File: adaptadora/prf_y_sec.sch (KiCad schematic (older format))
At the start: 35 parts, among them J18 Conn_Coaxial, J19 Conn_Coaxial, J20 Conn_Coaxial, J22 Conn_Coaxial, U13 LM361MX_NOPB, U14 LM361MX_NOPB, U23 TLV2772IDR, U32 SN74LVC2T45DCUR

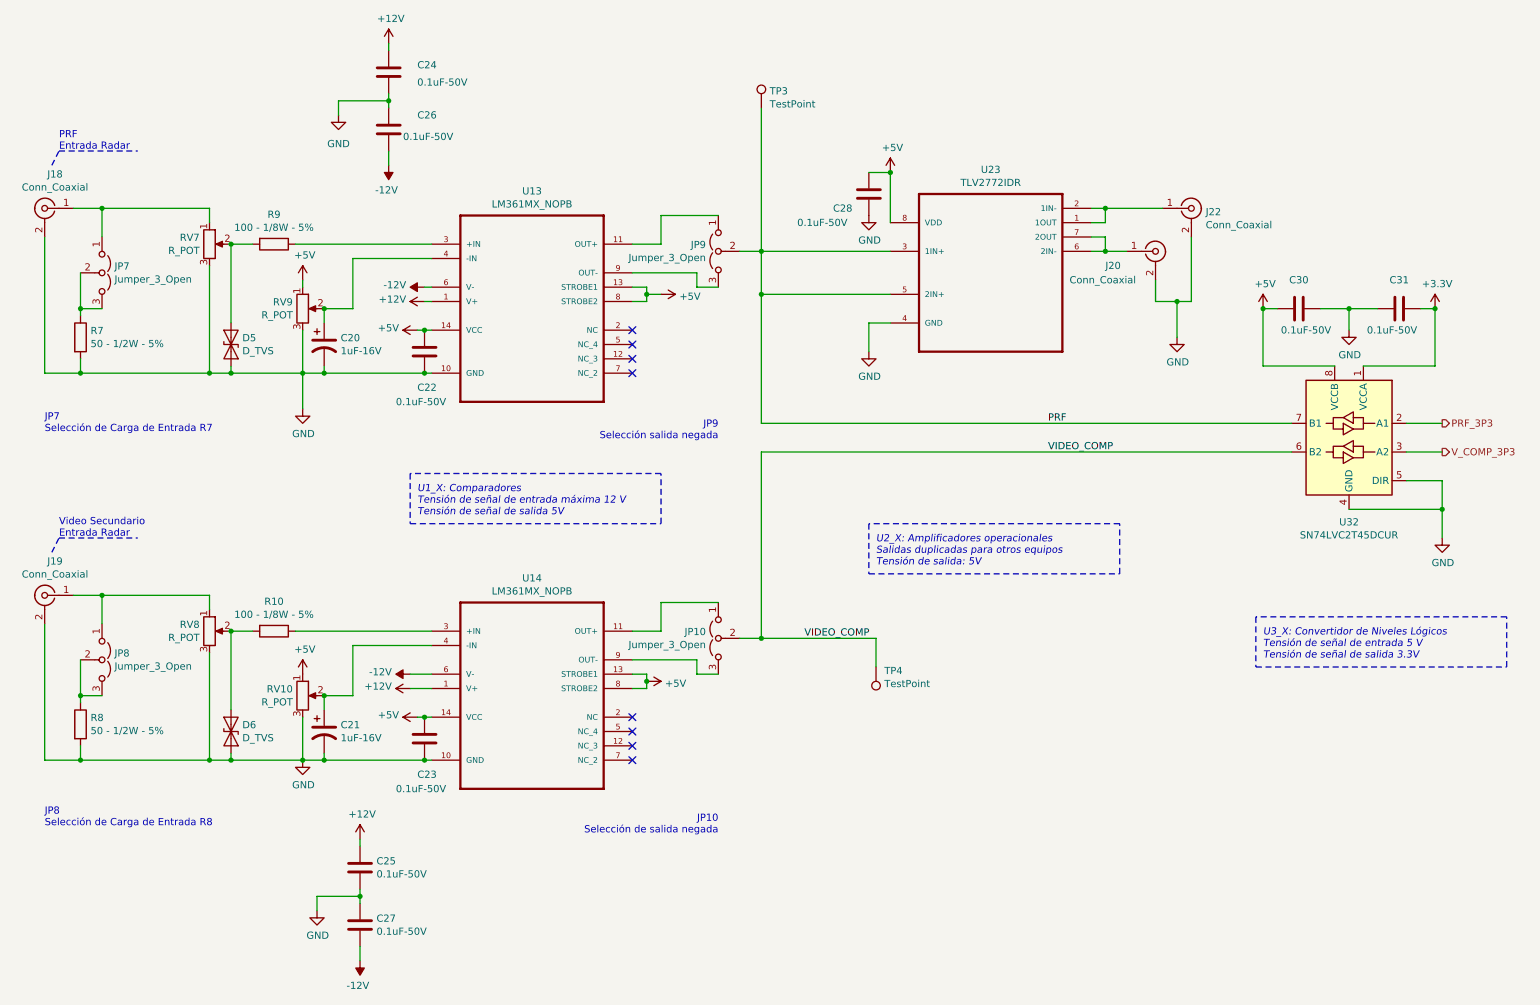
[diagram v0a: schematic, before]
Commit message: se ordenan campos de integrados
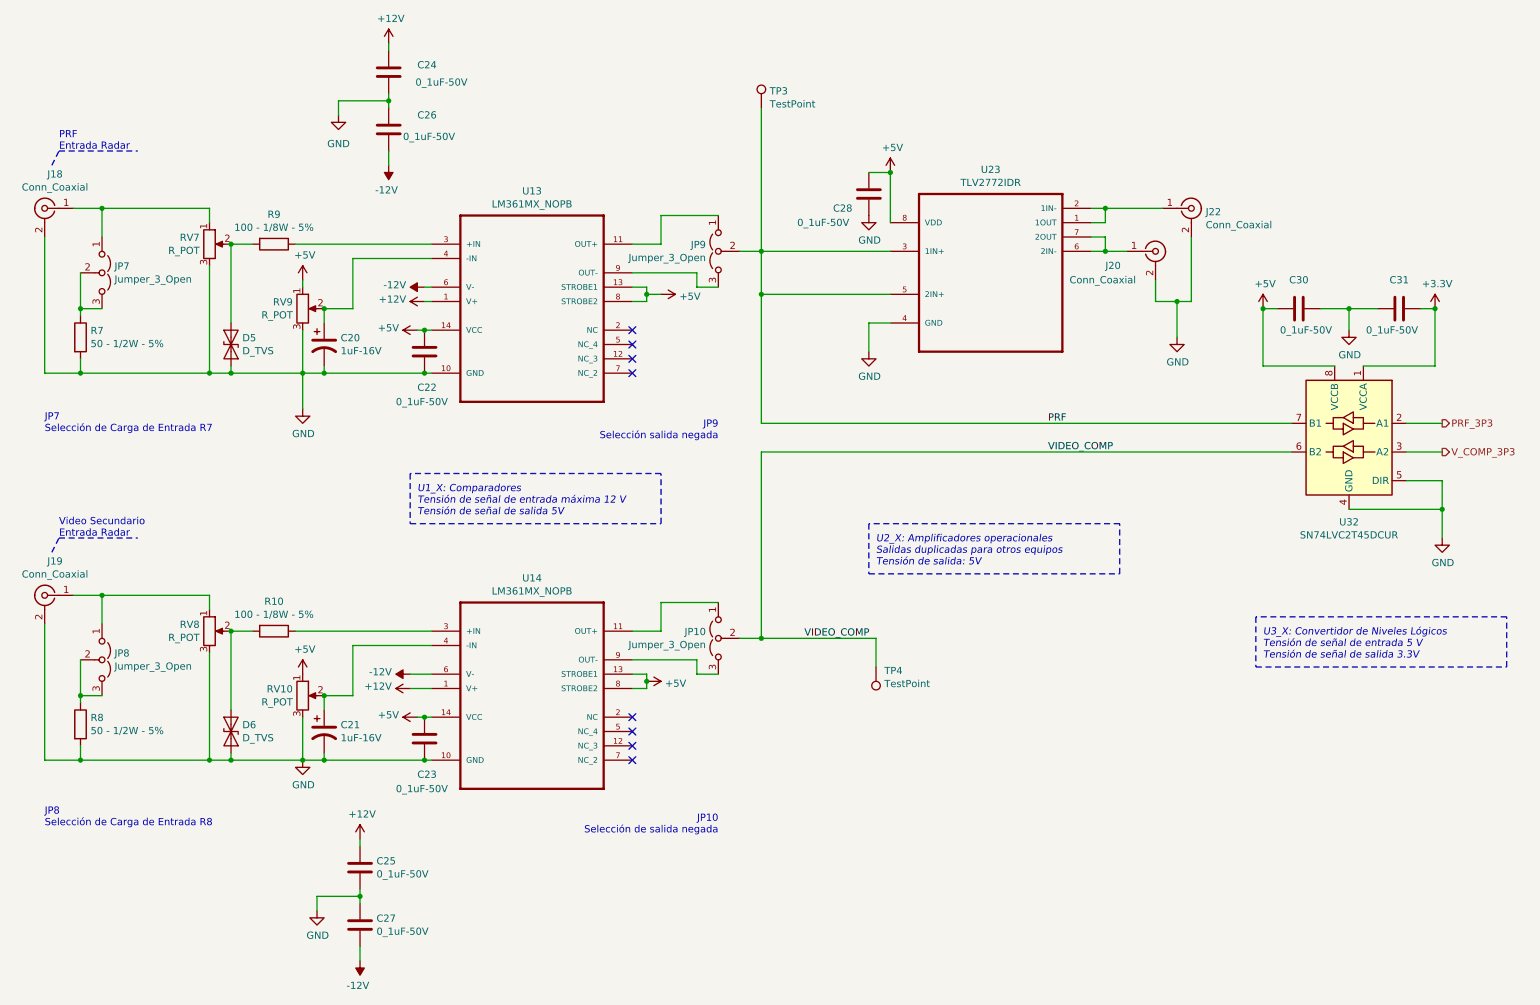
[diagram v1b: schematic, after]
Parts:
- C22, C23, C24, C25, C26, C27, C28, C30, C31: value 0.1uF-50V -> 0_1uF-50V
- U13, U14: Número de parte (Digi-Key) 296-47682-1-ND -> (none)
- U23: Campo4 Texas Instruments -> (none); Campo5 Dual 2.7-V High Slew Rate Rail-To-Rail Output Operational A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 -> (none); Campo6 TLV2772IDR -> (none); Campo7 https://www.digikey.com/product-detail/en/texas-instruments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 -> (none); Campo8 SOIC-8 Texas Instruments -> (none); Descripción (inglés) General Purpose Amplifier 2 Circuit Rail-to-Rail 8-SOIC -> Dual 2.7-V High Slew Rate Rail-To-Rail Output Operational A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; Número de parte (Digi-Key) 296-1902-2-ND -> (none)
- U32: Número de parte (Digi-Key) 296-17014-1-ND -> (none)
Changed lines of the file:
@@
 P 3350 2950
 F 0 "C22" H 3400 3200 50  0000 R CNN
-F 1 "0.1uF-50V" H 3550 3300 50  0000 R CNN
+F 1 "0_1uF-50V" H 3550 3300 50  0000 R CNN
 F 2 "Capacitor_SMD:C_0805_2012Metric" H 3388 2800 50  0001 C CNN
 F 3 "~" H 3350 2950 50  0001 C CNN
@@
 F 4 "Texas Instruments" H 4100 2500 50  0001 L BNN "Fabricante"
 F 5 "High Speed Differential Comparator 14-SOIC 0 to 70" H 4100 2500 50  0001 L BNN "Descripción (inglés)"
-F 6 "296-47682-1-ND" H 4100 2500 50  0001 L BNN "Número de parte (Digi-Key)"
+F 6 "296-47682-1-ND" H 4100 2500 50  0001 L BNN "Número de Parte (Digi-Key)"
 F 7 "https://www.digikey.com/product-detail/en/texas-instruments/LM361MX-NOPB/296-47682-1-ND/3526971" H 4100 2500 50  0001 L BNN "Enlace"
-F 8 "296-47682-1-ND" H 4100 2500 50  0001 C CNN "Número de Parte (Digi-Key)"
 	1    4100 2500
 	1    0    0    -1
@@
 P 3100 1000
 F 0 "C24" H 2900 1050 50  0000 R CNN
-F 1 "0.1uF-50V" H 2550 900 50  0000 L BNN
+F 1 "0_1uF-50V" H 2550 900 50  0000 L BNN
 F 2 "Capacitor_SMD:C_0805_2012Metric" H 3138 850 50  0001 C CNN
 F 3 "~" H 3100 1000 50  0001 C CNN
@@
 P 3100 1400
 F 0 "C26" H 3300 1500 50  0000 L CNN
-F 1 "0.1uF-50V" H 3200 1350 50  0000 L CNN
+F 1 "0_1uF-50V" H 3200 1350 50  0000 L CNN
 F 2 "Capacitor_SMD:C_0805_2012Metric" H 3138 1250 50  0001 C CNN
 F 3 "~" H 3100 1400 50  0001 C CNN
@@
 F 2 "Package_SO:SOIC-8_3.9x4.9mm_P1.27mm" H 7300 2250 50  0001 L BNN
 F 3 "http://www.ti.com/lit/ds/symlink/tlv2772.pdf" H 7300 2250 50  0001 L BNN
-F 4 "Texas Instruments" H 7300 2250 50  0001 L BNN "Campo4"
-F 5 "Dual 2.7-V High Slew Rate Rail-To-Rail Output Operational Amplifier 8-SOIC -40 to 125" H 7300 2250 50  0001 L BNN "Campo5"
-F 6 "TLV2772IDR" H 7300 2250 50  0001 L BNN "Campo6"
-F 7 "https://www.digikey.com/product-detail/en/texas-instruments/TLV2772IDR/296-1902-1-ND/405014?utm_source=snapeda&utm_medium=aggregator&utm_campaign=symbol" H 7300 2250 50  0001 L BNN "Campo7"
-F 8 "SOIC-8 Texas Instruments" H 7300 2250 50  0001 L BNN "Campo8"
-F 9 "General Purpose Amplifier 2 Circuit Rail-to-Rail 8-SOIC" H 7300 2250 50  0001 C CNN "Descripción (inglés)"
-F 10 "https://www.digikey.com/product-detail/en/texas-instruments/TLV2772IDR/296-1902-2-ND/374332" H 7300 2250 50  0001 C CNN "Enlace"
-F 11 "Texas Instruments" H 7300 2250 50  0001 C CNN "Fabricante"
-F 12 "296-1902-2-ND" H 7300 2250 50  0001 C CNN "Número de Parte (Digi-Key)"
-F 13 "296-1902-2-ND" H 7300 2250 50  0001 C CNN "Número de parte (Digi-Key)"
+F 4 "Dual 2.7-V High Slew Rate Rail-To-Rail Output Operational Amplifier 8-SOIC -40 to 125" H 7300 2250 50  0001 C CNN "Descripción (inglés)"
+F 5 "Texas Instruments" H 7300 2250 50  0001 C CNN "Fabricante"
+F 6 "296-1902-2-ND" H 7300 2250 50  0001 C CNN "Número de Parte (Digi-Key)"
+F 7 "https://www.digikey.com/product-detail/en/texas-instruments/TLV2772IDR/296-1902-2-ND/374332" H 7300 2250 50  0001 C CNN "Enlace"
 	1    7300 2250
 	1    0    0    -1
@@
 P 10150 2650
 F 0 "C31" V 9950 2650 50  0000 C CNN
-F 1 "0.1uF-50V" V 10300 2600 50  0000 C CNN
+F 1 "0_1uF-50V" V 10300 2600 50  0000 C CNN
 F 2 "Capacitor_SMD:C_0805_2012Metric" H 10188 2500 50  0001 C CNN
 F 3 "~" H 10150 2650 50  0001 C CNN
@@
 F 3 "http://www.ti.com/lit/ds/symlink/sn74lvc2t45.pdf" H 8900 3000 50  0001 C CNN
 F 4 "Dual-Bit Dual-Supply Bus Transceiver With Configurable Voltage" H 9800 3550 50  0001 C CNN "Descripción (inglés)"
-F 5 "https://www.digikey.com/product-detail/en/texas-instruments/SN74LVC2T45DCUR/296-17014-2-ND/657833" H 9800 3550 50  0001 C CNN "Enlace"
-F 6 "Texas Instruments" H 9800 3550 50  0001 C CNN "Fabricante"
-F 7 "296-17014-1-ND" H 9800 3550 50  0001 C CNN "Número de Parte (Digi-Key)"
-F 8 "296-17014-1-ND" H 9800 3550 50  0001 C CNN "Número de parte (Digi-Key)"
+F 5 "Texas Instruments" H 9800 3550 50  0001 C CNN "Fabricante"
+F 6 "296-17014-1-ND" H 9800 3550 50  0001 C CNN "Número de Parte (Digi-Key)"
+F 7 "https://www.digikey.com/product-detail/en/texas-instruments/SN74LVC2T45DCUR/296-17014-2-ND/657833" H 9800 3550 50  0001 C CNN "Enlace"
 	1    9800 3550
 	-1   0    0    -1
@@
 P 6450 1850
 F 0 "C28" H 6200 1750 50  0000 L CNN
-F 1 "0.1uF-50V" H 5950 1650 50  0000 L CNN
+F 1 "0_1uF-50V" H 5950 1650 50  0000 L CNN
 F 2 "Capacitor_SMD:C_0805_2012Metric" H 6488 1700 50  0001 C CNN
 F 3 "~" H 6450 1850 50  0001 C CNN
@@
 P 3350 5650
 F 0 "C23" H 3400 5900 50  0000 R CNN
-F 1 "0.1uF-50V" H 3550 6000 50  0000 R CNN
+F 1 "0_1uF-50V" H 3550 6000 50  0000 R CNN
 F 2 "Capacitor_SMD:C_0805_2012Metric" H 3388 5500 50  0001 C CNN
 F 3 "~" H 3350 5650 50  0001 C CNN
@@
 F 4 "Texas Instruments" H 4100 5200 50  0001 L BNN "Fabricante"
 F 5 "High Speed Differential Comparator 14-SOIC 0 to 70" H 4100 5200 50  0001 L BNN "Descripción (inglés)"
-F 6 "296-47682-1-ND" H 4100 5200 50  0001 L BNN "Número de parte (Digi-Key)"
+F 6 "296-47682-1-ND" H 4100 5200 50  0001 L BNN "Número de Parte (Digi-Key)"
 F 7 "https://www.digikey.com/product-detail/en/texas-instruments/LM361MX-NOPB/296-47682-1-ND/3526971" H 4100 5200 50  0001 L BNN "Enlace"
-F 8 "296-47682-1-ND" H 4100 5200 50  0001 C CNN "Número de Parte (Digi-Key)"
 	1    4100 5200
 	1    0    0    -1
@@
 P 2900 6550
 F 0 "C25" H 2785 6596 50  0000 R CNN
-F 1 "0.1uF-50V" H 2785 6505 50  0000 R CNN
+F 1 "0_1uF-50V" H 2785 6505 50  0000 R CNN
 F 2 "Capacitor_SMD:C_0805_2012Metric" H 2938 6400 50  0001 C CNN
 F 3 "~" H 2900 6550 50  0001 C CNN
@@
 P 2900 6950
 F 0 "C27" H 3015 6996 50  0000 L CNN
-F 1 "0.1uF-50V" H 3015 6905 50  0000 L CNN
+F 1 "0_1uF-50V" H 3015 6905 50  0000 L CNN
 F 2 "Capacitor_SMD:C_0805_2012Metric" H 2938 6800 50  0001 C CNN
 F 3 "~" H 2900 6950 50  0001 C CNN
@@
 P 9450 2650
 F 0 "C30" V 9250 2650 50  0000 C CNN
-F 1 "0.1uF-50V" V 9600 2700 50  0000 C CNN
+F 1 "0_1uF-50V" V 9600 2700 50  0000 C CNN
 F 2 "Capacitor_SMD:C_0805_2012Metric" H 9488 2500 50  0001 C CNN
 F 3 "~" H 9450 2650 50  0001 C CNN

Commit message: se cambia footprint de componentes y el posicionamiento
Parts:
- D5, D6: footprint Diode_SMD:D_0201_0603Metric -> Diode_THT:D_DO-15_P10.16mm_Horizontal
- JP10, JP7, JP8, JP9: footprint Jumper:SolderJumper-3_P1.3mm_Open_Pad1.0x1.5mm_NumberLabels -> Connector_PinHeader_2.54mm:PinHeader_1x03_P2.54mm_Vertical
- U13, U14: footprint Package_SO:SOIC-14_3.9x8.7mm_P1.27mm -> Package_DIP:DIP-14_W7.62mm_Socket
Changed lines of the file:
@@
 F 0 "D5" V 1954 2979 50  0000 L CNN
 F 1 "D_TVS" V 2045 2979 50  0000 L CNN
-F 2 "Diode_SMD:D_0201_0603Metric" H 2000 2900 50  0001 C CNN
+F 2 "Diode_THT:D_DO-15_P10.16mm_Horizontal" H 2000 2900 50  0001 C CNN
 F 3 "~" H 2000 2900 50  0001 C CNN
 	1    2000 2900
@@
 F 0 "JP7" V 1054 2487 50  0000 L CNN
 F 1 "Jumper_3_Open" V 1145 2487 50  0000 L CNN
-F 2 "Jumper:SolderJumper-3_P1.3mm_Open_Pad1.0x1.5mm_NumberLabels" H 1100 2400 50  0001 C CNN
+F 2 "Connector_PinHeader_2.54mm:PinHeader_1x03_P2.54mm_Vertical" H 1100 2400 50  0001 C CNN
 F 3 "~" H 1100 2400 50  0001 C CNN
 	1    1100 2400
@@
 F 0 "U13" H 4100 3170 50  0000 C CNN
 F 1 "LM361MX_NOPB" H 4100 3079 50  0000 C CNN
-F 2 "Package_SO:SOIC-14_3.9x8.7mm_P1.27mm" H 4100 2500 50  0001 L BNN
+F 2 "Package_DIP:DIP-14_W7.62mm_Socket" H 4100 2500 50  0001 L BNN
 F 3 "http://www.ti.com/lit/ds/symlink/lm361.pdf" H 4100 2500 50  0001 L BNN
 F 4 "Texas Instruments" H 4100 2500 50  0001 L BNN "Fabricante"
@@
 F 0 "JP9" V 5354 2337 50  0000 L CNN
 F 1 "Jumper_3_Open" V 5445 2337 50  0000 L CNN
-F 2 "Jumper:SolderJumper-3_P1.3mm_Open_Pad1.0x1.5mm_NumberLabels" H 5400 2250 50  0001 C CNN
+F 2 "Connector_PinHeader_2.54mm:PinHeader_1x03_P2.54mm_Vertical" H 5400 2250 50  0001 C CNN
 F 3 "~" H 5400 2250 50  0001 C CNN
 	1    5400 2250
@@
 F 0 "D6" V 1954 5679 50  0000 L CNN
 F 1 "D_TVS" V 2045 5679 50  0000 L CNN
-F 2 "Diode_SMD:D_0201_0603Metric" H 2000 5600 50  0001 C CNN
+F 2 "Diode_THT:D_DO-15_P10.16mm_Horizontal" H 2000 5600 50  0001 C CNN
 F 3 "~" H 2000 5600 50  0001 C CNN
 	1    2000 5600
@@
 F 0 "JP8" V 1054 5187 50  0000 L CNN
 F 1 "Jumper_3_Open" V 1145 5187 50  0000 L CNN
-F 2 "Jumper:SolderJumper-3_P1.3mm_Open_Pad1.0x1.5mm_NumberLabels" H 1100 5100 50  0001 C CNN
+F 2 "Connector_PinHeader_2.54mm:PinHeader_1x03_P2.54mm_Vertical" H 1100 5100 50  0001 C CNN
 F 3 "~" H 1100 5100 50  0001 C CNN
 	1    1100 5100
@@
 F 0 "U14" H 4100 5870 50  0000 C CNN
 F 1 "LM361MX_NOPB" H 4100 5779 50  0000 C CNN
-F 2 "Package_SO:SOIC-14_3.9x8.7mm_P1.27mm" H 4100 5200 50  0001 L BNN
+F 2 "Package_DIP:DIP-14_W7.62mm_Socket" H 4100 5200 50  0001 L BNN
 F 3 "http://www.ti.com/lit/ds/symlink/lm361.pdf" H 4100 5200 50  0001 L BNN
 F 4 "Texas Instruments" H 4100 5200 50  0001 L BNN "Fabricante"
@@
 F 0 "JP10" V 5354 5037 50  0000 L CNN
 F 1 "Jumper_3_Open" V 5445 5037 50  0000 L CNN
-F 2 "Jumper:SolderJumper-3_P1.3mm_Open_Pad1.0x1.5mm_NumberLabels" H 5400 4950 50  0001 C CNN
+F 2 "Connector_PinHeader_2.54mm:PinHeader_1x03_P2.54mm_Vertical" H 5400 4950 50  0001 C CNN
 F 3 "~" H 5400 4950 50  0001 C CNN
 	1    5400 4950

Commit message: modificaciones bom
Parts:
- U13, U14: Descripción (inglés) High Speed Differential Comparator 14-SOIC 0 to 70 -> High Speed Differential Comparator; Enlace https://www.digikey.com/product-detail/en/texas-instruments/LM361MX-NOPB/296-47682-1-ND/3526971 -> https://www.digikey.com/product-detail/en/texas-instruments/LM361N-NOPB/LM361N-NOPB-ND/32491; Número de Parte (Digi-Key) 296-47682-1-ND -> LM361N/NOPB-ND
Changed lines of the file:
@@
 F 3 "http://www.ti.com/lit/ds/symlink/lm361.pdf" H 4100 2500 50  0001 L BNN
 F 4 "Texas Instruments" H 4100 2500 50  0001 L BNN "Fabricante"
-F 5 "High Speed Differential Comparator 14-SOIC 0 to 70" H 4100 2500 50  0001 L BNN "Descripción (inglés)"
-F 6 "296-47682-1-ND" H 4100 2500 50  0001 L BNN "Número de Parte (Digi-Key)"
-F 7 "https://www.digikey.com/product-detail/en/texas-instruments/LM361MX-NOPB/296-47682-1-ND/3526971" H 4100 2500 50  0001 L BNN "Enlace"
+F 5 "High Speed Differential Comparator" H 4100 2500 50  0001 L BNN "Descripción (inglés)"
+F 6 "LM361N/NOPB-ND" H 4100 2500 50  0001 L BNN "Número de Parte (Digi-Key)"
+F 7 "https://www.digikey.com/product-detail/en/texas-instruments/LM361N-NOPB/LM361N-NOPB-ND/32491" H 4100 2500 50  0001 L BNN "Enlace"
 	1    4100 2500
 	1    0    0    -1
@@
 F 3 "http://www.ti.com/lit/ds/symlink/lm361.pdf" H 4100 5200 50  0001 L BNN
 F 4 "Texas Instruments" H 4100 5200 50  0001 L BNN "Fabricante"
-F 5 "High Speed Differential Comparator 14-SOIC 0 to 70" H 4100 5200 50  0001 L BNN "Descripción (inglés)"
-F 6 "296-47682-1-ND" H 4100 5200 50  0001 L BNN "Número de Parte (Digi-Key)"
-F 7 "https://www.digikey.com/product-detail/en/texas-instruments/LM361MX-NOPB/296-47682-1-ND/3526971" H 4100 5200 50  0001 L BNN "Enlace"
+F 5 "High Speed Differential Comparator" H 4100 5200 50  0001 L BNN "Descripción (inglés)"
+F 6 "LM361N/NOPB-ND" H 4100 5200 50  0001 L BNN "Número de Parte (Digi-Key)"
+F 7 "https://www.digikey.com/product-detail/en/texas-instruments/LM361N-NOPB/LM361N-NOPB-ND/32491" H 4100 5200 50  0001 L BNN "Enlace"
 	1    4100 5200
 	1    0    0    -1
